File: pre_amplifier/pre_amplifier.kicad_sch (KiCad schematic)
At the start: 17 parts, among them J1 IN, J2 OUT, J3 35V, Q1 2N3904, Q2 2N3904

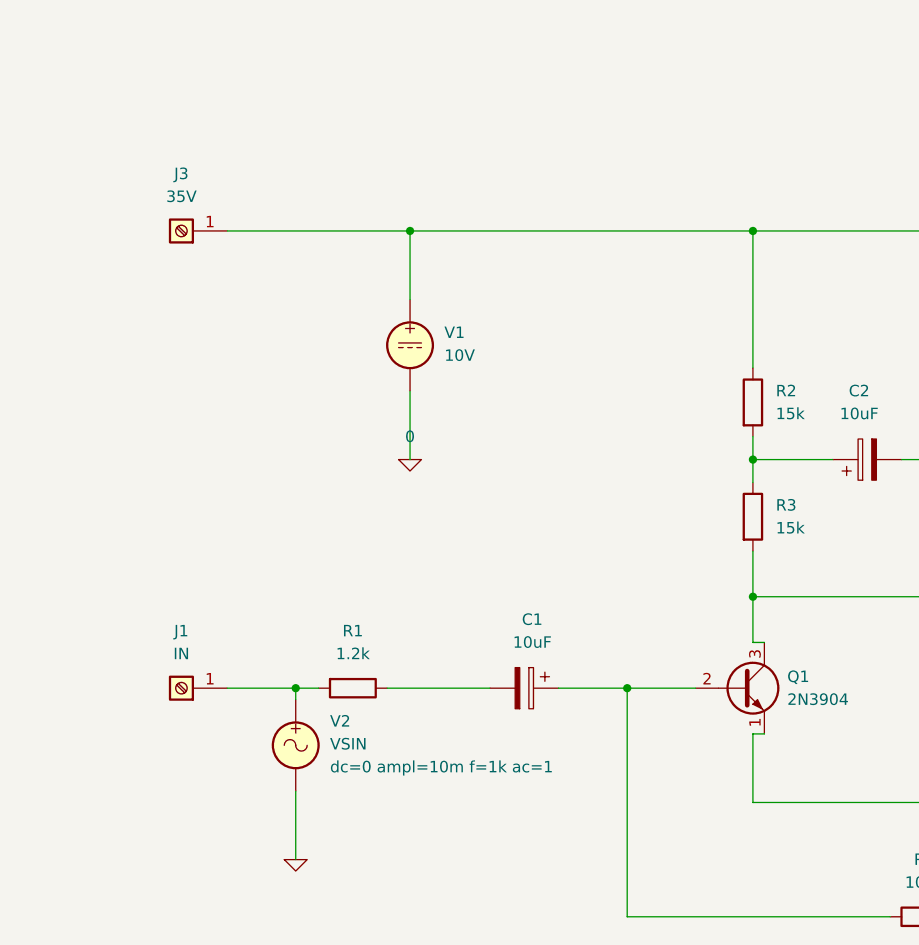
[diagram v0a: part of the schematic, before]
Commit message: 40V upgrade and generate BOM CSVs
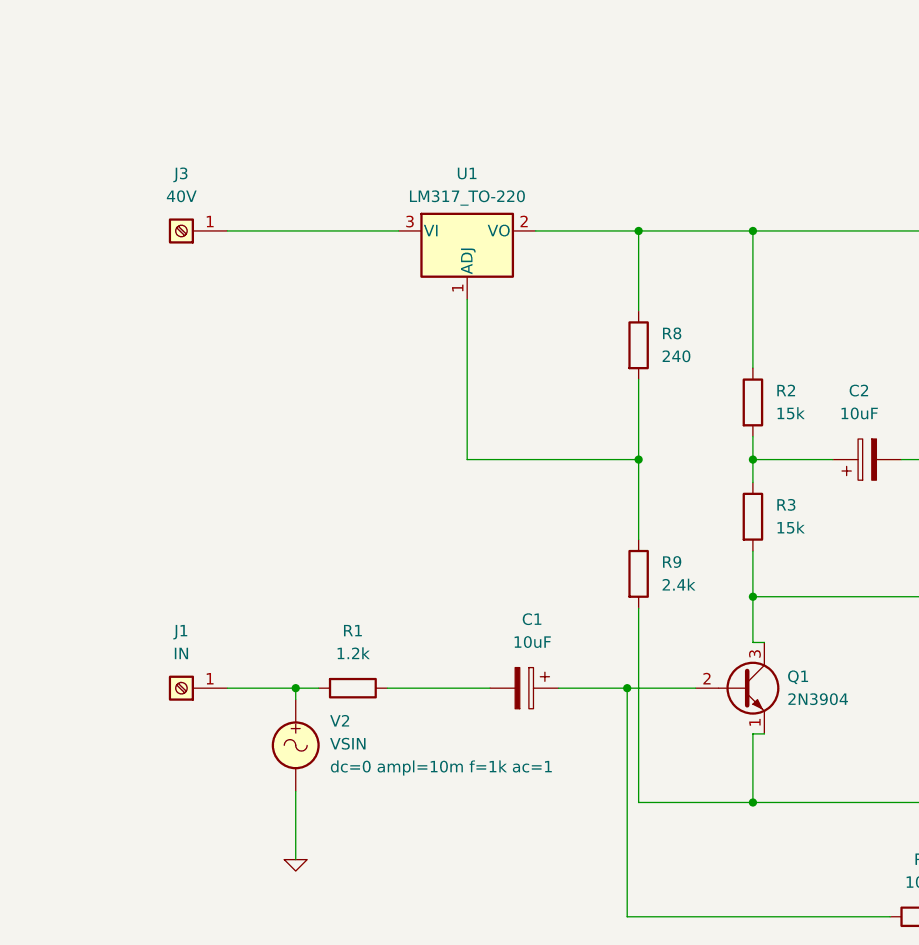
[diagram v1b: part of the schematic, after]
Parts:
- removed V1: 10V, symbol Simulation_SPICE:VDC
- added R8: 240, symbol Device:R
- added R9: 2.4k, symbol Device:R
- added U1: LM317_TO-220, Package_TO_SOT_THT:TO-220-3_Vertical, symbol Regulator_Linear:LM317_TO-220
- J3: value 35V -> 40V
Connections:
- net 0: now also R9.2
- net at Q2.3 (C), R2.1: now also R8.1, U1.2 (VO); no longer J3.1 (Pin_1)
- new net: R8.2, R9.1, U1.1 (ADJ)
- new net: J3.1 (Pin_1), U1.3 (VI)
